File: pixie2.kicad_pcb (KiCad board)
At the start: 2 copper layers, 75 x 46 mm, 45 parts, among them J1 Conn_Coaxial, J2 AudioJack2, Q1 BC547, Q2 2N2219, SW1 SW_Push, U1 LM386, Y1 3579kHz

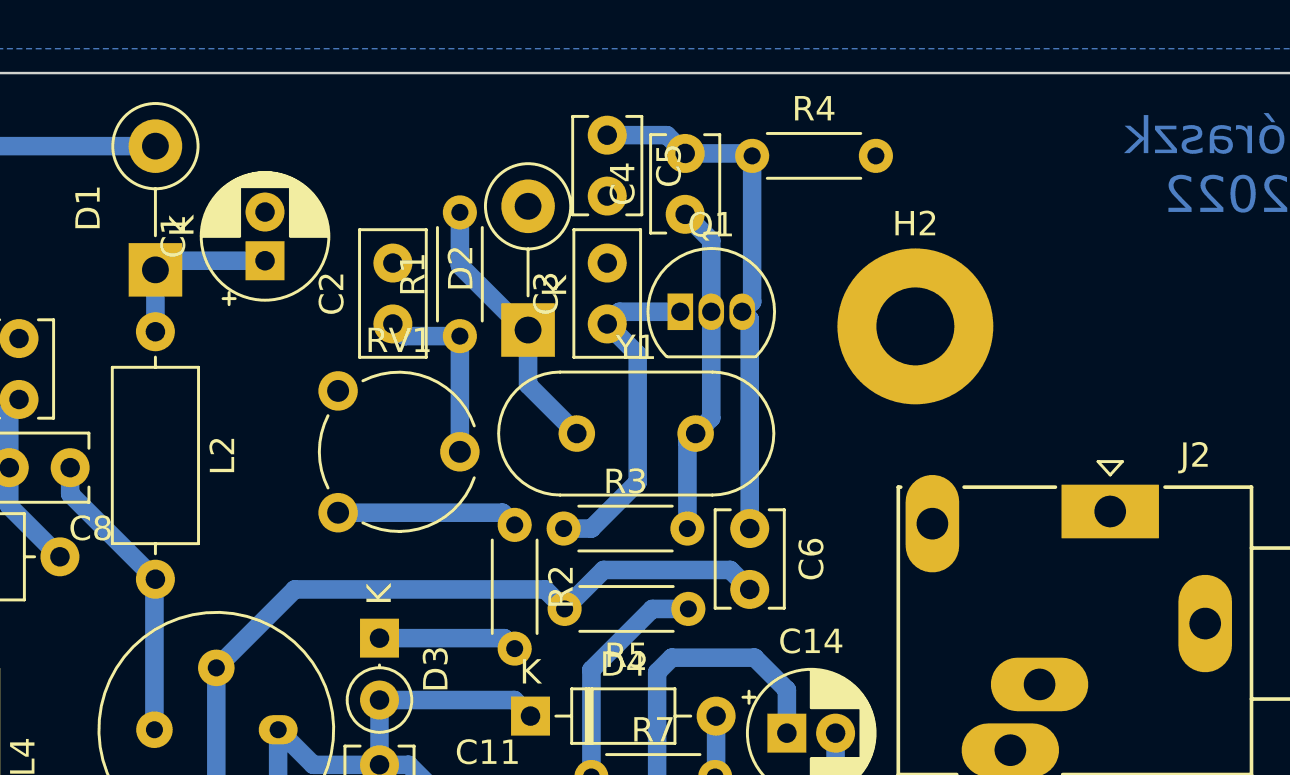
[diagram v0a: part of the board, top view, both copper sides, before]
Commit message: fix vcc line
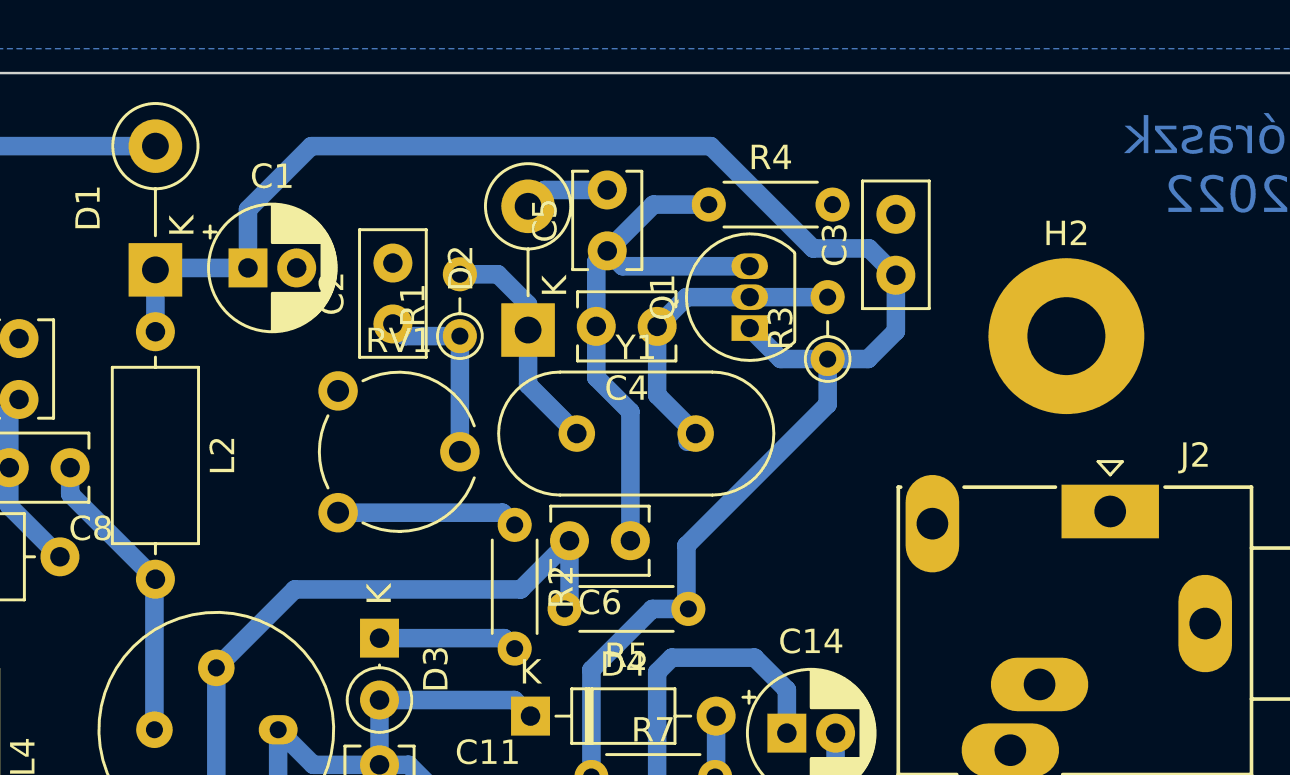
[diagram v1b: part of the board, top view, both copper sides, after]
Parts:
- R1, R3: footprint Resistor_THT:R_Axial_DIN0204_L3.6mm_D1.6mm_P5.08mm_Horizontal -> Resistor_THT:R_Axial_DIN0204_L3.6mm_D1.6mm_P2.54mm_Vertical
- moved R3 12.9 mm to (136.6, 55.7), turned to 90 degrees
- moved C3 12.0 mm to (139.4, 52.3)
- moved H2 6.21 mm to (146.4, 54.8)
- moved C6 4.93 mm to (128.5, 63.2), turned to 180 degrees
- moved C5 4.75 mm to (127.5, 51.3), turned to 90 degrees
- moved C4 4.74 mm to (129.6, 54.4), turned to 180 degrees
- moved Q1 2.93 mm to (133.4, 54.5), turned to 90 degrees
- moved R4 2.68 mm to (131.7, 49.4)
- moved C1 0.76 mm to (112.8, 52.0), turned to 0 degrees
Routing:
- net VCC: track 30.7 -> 70.6 mm
- net Net-(C6-Pad2): track 35.4 -> 30.4 mm
- net GND: track 0.00 -> 3.53 mm
- net Net-(C4-Pad2): track 21.9 -> 23.7 mm
- net Net-(D2-Pad1): track 11.2 -> 9.59 mm
- net Net-(C4-Pad1): track 13.7 -> 13.0 mm

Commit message: Finalize
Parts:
- added REF**: MountingHole_2.5mm, MountingHole:MountingHole_2.5mm, F.Cu at (87.8, 50.0)
- L4: footprint Inductor_THT:L_Axial_L7.0mm_D3.3mm_P10.16mm_Horizontal_Fastron_MICC -> Inductor_THT:L_Axial_L7.0mm_D3.3mm_P5.08mm_Vertical_Fastron_MICC
- moved H1 12.8 mm to (89.0, 85.0)
- moved J1 6.72 mm to (99.6, 79.8)
- moved C16 5.83 mm to (141.0, 83.4)
- moved C17 4.73 mm to (139.6, 77.8), turned to 90 degrees
- moved H3 3.96 mm to (154.0, 85.0)
- moved L4 0.80 mm to (100.8, 67.8)
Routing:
- net Net-(C17-Pad2): track 0.00 -> 18.9 mm
- net GND: track 3.53 -> 22.3 mm
- net Net-(C16-Pad1): track 18.1 -> 29.4 mm
- net Net-(C17-Pad1): track 3.89 -> 8.20 mm
- net Net-(C13-Pad2): track 16.2 -> 14.2 mm
- net Net-(D2-Pad1): track 9.59 -> 8.39 mm
- net VCC: track 70.6 -> 70.1 mm

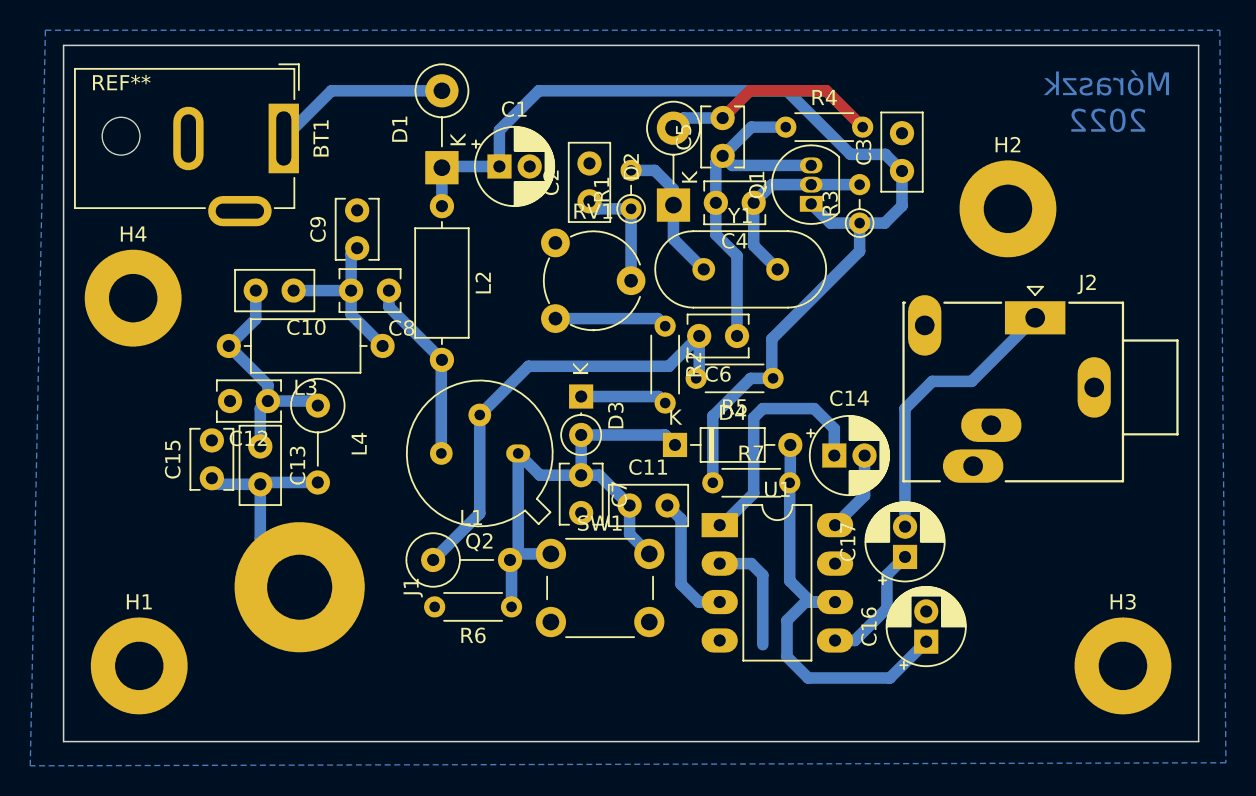
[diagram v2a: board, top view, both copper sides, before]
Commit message: Edge.Cuts decrease
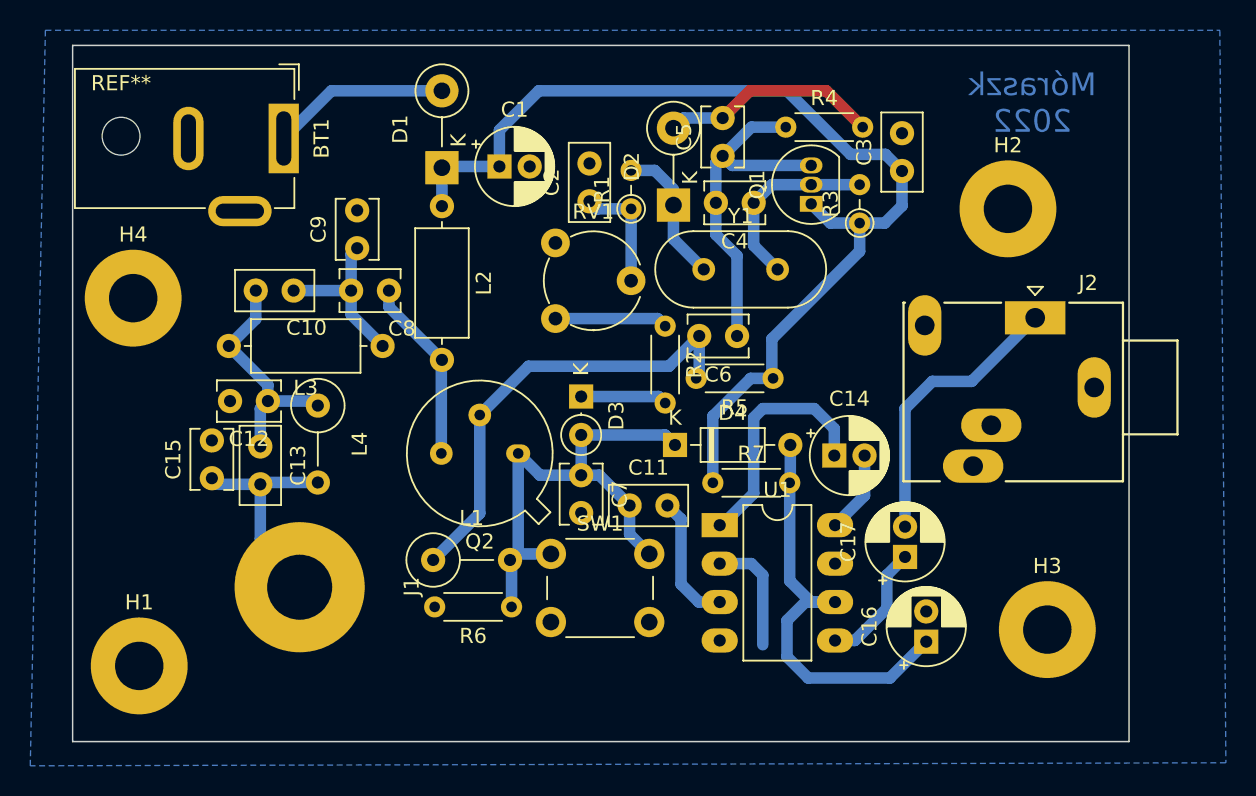
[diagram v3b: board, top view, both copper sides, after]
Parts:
- moved H3 5.55 mm to (149.0, 82.6)
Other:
- board size 75 x 46 mm -> 69.8 x 46 mm
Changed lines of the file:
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@@
   )
   (footprint "MountingHole:MountingHole_3.2mm_M3_Pad" (layer "F.Cu")
-    (at 154 85)
+    (at 149 82.6)
     (descr "Mounting Hole 3.2mm, M3")
     (tags "mounting hole 3.2mm m3")
@@
     )
   )
-  (gr_line (start 84 90) (end 84 44) (layer "Edge.Cuts") (width 0.1))
-  (gr_line (start 159 90) (end 84 90) (layer "Edge.Cuts") (width 0.1))
-  (gr_line (start 84 44) (end 159 44) (layer "Edge.Cuts") (width 0.1))
-  (gr_line (start 84 44) (end 84 44) (layer "Edge.Cuts") (width 0.1))
-  (gr_line (start 159 44) (end 159 90) (layer "Edge.Cuts") (width 0.1))
-  (gr_text "Móraszk\n2022" (at 153 47.8) (layer "B.Cu")
+  (gr_line (start 84.6 90) (end 84.6 44) (layer "Edge.Cuts") (width 0.1))
+  (gr_line (start 154.4 90) (end 84.6 90) (layer "Edge.Cuts") (width 0.1))
+  (gr_line (start 84.6 44) (end 154.4 44) (layer "Edge.Cuts") (width 0.1))
+  (gr_line (start 154.4 44) (end 154.4 90) (layer "Edge.Cuts") (width 0.1))
+  (gr_text "Móraszk\n2022" (at 148 47.8) (layer "B.Cu")
     (effects (font (size 1.5 1.5) (thickness 0.3)) (justify mirror))
   )
